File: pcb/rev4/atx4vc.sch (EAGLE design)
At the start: 58 parts, among them IC1 MY_7905DT, IC2 MAX486X/SOT, J2 ATX24RH

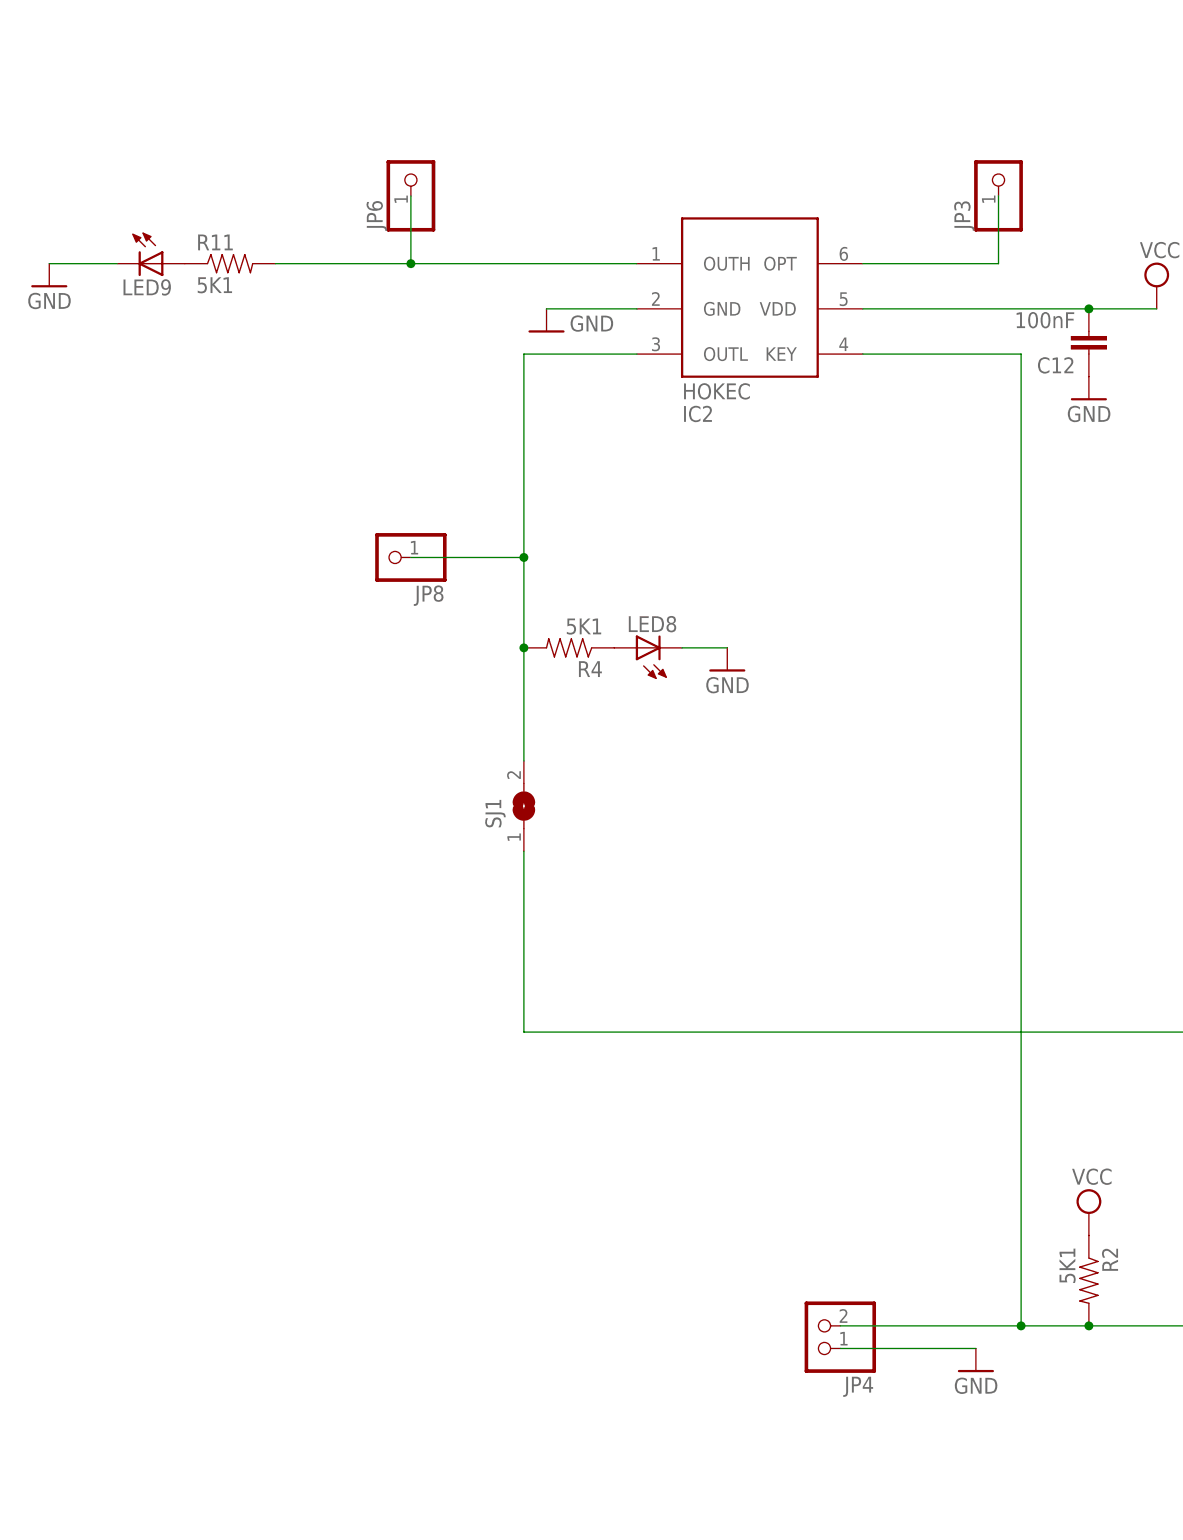
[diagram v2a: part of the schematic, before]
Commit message: soft power ic tested working
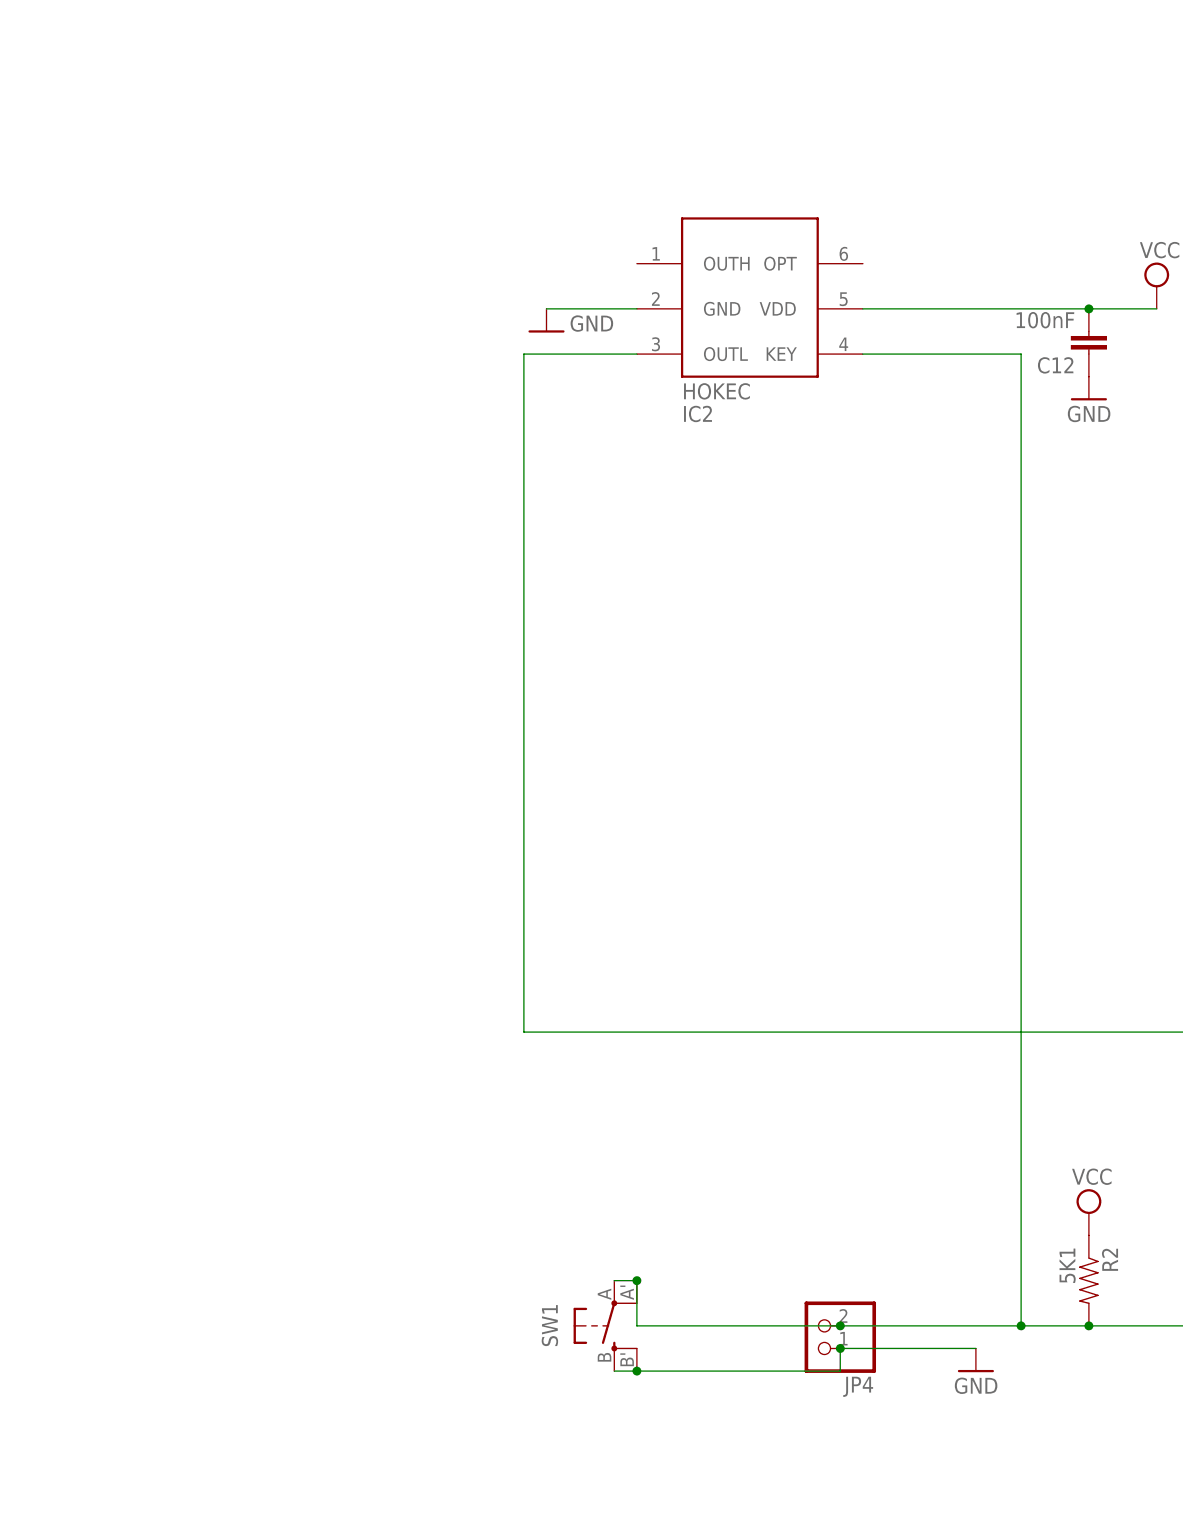
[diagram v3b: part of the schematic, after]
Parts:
- removed JP3, JP6, JP8: (no value), adafruit_changed:PINHD-1X1CB
- removed LED8, LED9: (no value), adafruit:LEDCHIP-LED0805
- removed R11, R4: 5K1, atx_power_control:RESISTOR0805-RES
- removed SJ1: (no value), jumper:SJ
- added SW1: SPST_TACT-EVQQ2, duckypad:SPST_TACT-EVQQ2
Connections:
- removed net N$13: LED8.A, R4.1
- removed net N$16: LED9.A, R11.1
- removed net N$19: IC2.OUTL, JP8.1, R4.2, SJ1.2
- removed net N$3: IC2.OPT, JP3.1
- removed net N$7: IC2.OUTH, JP6.1, R11.2
- net GND: now also SW1.S, SW1.S1; no longer LED8.C, LED9.C
- net N$12: now also SW1.P, SW1.P1
- net N$6: now also IC2.OUTL; no longer SJ1.1
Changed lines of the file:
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@@
 <part name="R2" library="atx_power_control" deviceset="RESISTOR" device="0805-RES" value="5K1"/>
 <part name="SUPPLY7" library="supply2" library_urn="urn:adsk.eagle:library:372" deviceset="VCC" device=""/>
-<part name="R4" library="atx_power_control" deviceset="RESISTOR" device="0805-RES" value="5K1"/>
-<part name="LED8" library="adafruit" deviceset="LED" device="CHIP-LED0805"/>
-<part name="GND27" library="supply1" deviceset="GND" device=""/>
-<part name="R11" library="atx_power_control" deviceset="RESISTOR" device="0805-RES" value="5K1"/>
-<part name="LED9" library="adafruit" deviceset="LED" device="CHIP-LED0805"/>
-<part name="GND28" library="supply1" deviceset="GND" device=""/>
-<part name="JP6" library="adafruit_changed" deviceset="PINHD-1X1" device="CB"/>
-<part name="JP8" library="adafruit_changed" deviceset="PINHD-1X1" device="CB"/>
-<part name="SJ1" library="jumper" library_urn="urn:adsk.eagle:library:252" deviceset="SJ" device="" package3d_urn="urn:adsk.eagle:package:15471/1"/>
-<part name="JP3" library="adafruit_changed" deviceset="PINHD-1X1" device="CB"/>
+<part name="SW1" library="duckypad" deviceset="SPST_TACT" device="-EVQQ2"/>
 </parts>
 <sheets>
@@
 <attribute name="VALUE" x="158.115" y="-19.685" size="1.778" layer="96"/>
 </instance>
-<instance part="R4" gate="G$1" x="101.6" y="40.64" smashed="yes" rot="R180">
-<attribute name="NAME" x="105.41" y="39.1414" size="1.778" layer="95" rot="R180"/>
-<attribute name="VALUE" x="105.41" y="43.942" size="1.778" layer="96" rot="R180"/>
-</instance>
-<instance part="LED8" gate="G$1" x="109.22" y="40.64" smashed="yes" rot="R90">
-<attribute name="NAME" x="113.792" y="44.196" size="1.778" layer="95" rot="R180"/>
-<attribute name="VALUE" x="113.792" y="46.355" size="1.778" layer="96" rot="R180"/>
-</instance>
-<instance part="GND27" gate="1" x="119.38" y="38.1" smashed="yes" rot="MR0">
-<attribute name="VALUE" x="121.92" y="35.56" size="1.778" layer="96" rot="MR0"/>
-</instance>
-<instance part="R11" gate="G$1" x="63.5" y="83.82" smashed="yes">
-<attribute name="NAME" x="59.69" y="85.3186" size="1.778" layer="95"/>
-<attribute name="VALUE" x="59.69" y="80.518" size="1.778" layer="96"/>
-</instance>
-<instance part="LED9" gate="G$1" x="55.88" y="83.82" smashed="yes" rot="R270">
-<attribute name="NAME" x="51.308" y="80.264" size="1.778" layer="95"/>
-<attribute name="VALUE" x="51.308" y="78.105" size="1.778" layer="96"/>
-</instance>
-<instance part="GND28" gate="1" x="43.18" y="81.28" smashed="yes" rot="MR0">
-<attribute name="VALUE" x="45.72" y="78.74" size="1.778" layer="96" rot="MR0"/>
-</instance>
-<instance part="JP6" gate="G$1" x="83.82" y="93.98" smashed="yes" rot="R90">
-<attribute name="NAME" x="80.645" y="87.63" size="1.778" layer="95" rot="R90"/>
-<attribute name="VALUE" x="88.9" y="87.63" size="1.778" layer="96" rot="R90"/>
-</instance>
-<instance part="JP8" gate="G$1" x="81.28" y="50.8" smashed="yes" rot="R180">
-<attribute name="NAME" x="87.63" y="47.625" size="1.778" layer="95" rot="R180"/>
-<attribute name="VALUE" x="87.63" y="55.88" size="1.778" layer="96" rot="R180"/>
-</instance>
-<instance part="SJ1" gate="1" x="96.52" y="22.86" smashed="yes" rot="R90">
-<attribute name="NAME" x="93.98" y="20.32" size="1.778" layer="95" rot="R90"/>
-<attribute name="VALUE" x="100.33" y="20.32" size="1.778" layer="96" rot="R90"/>
-</instance>
-<instance part="JP3" gate="G$1" x="149.86" y="93.98" smashed="yes" rot="R90">
-<attribute name="NAME" x="146.685" y="87.63" size="1.778" layer="95" rot="R90"/>
-<attribute name="VALUE" x="154.94" y="87.63" size="1.778" layer="96" rot="R90"/>
+<instance part="SW1" gate="G$1" x="106.68" y="-35.56" smashed="yes" rot="MR180">
+<attribute name="NAME" x="100.33" y="-33.02" size="1.778" layer="95" rot="MR270"/>
 </instance>
 </instances>
@@
 <pinref part="JP4" gate="G$1" pin="1"/>
 <wire x1="147.32" y1="-38.1" x2="132.08" y2="-38.1" width="0.1524" layer="91"/>
+<pinref part="SW1" gate="G$1" pin="S"/>
+<pinref part="SW1" gate="G$1" pin="S1"/>
+<wire x1="106.68" y1="-40.64" x2="109.22" y2="-40.64" width="0.1524" layer="91"/>
+<wire x1="132.08" y1="-38.1" x2="132.08" y2="-40.64" width="0.1524" layer="91"/>
+<wire x1="132.08" y1="-40.64" x2="109.22" y2="-40.64" width="0.1524" layer="91"/>
+<junction x="132.08" y="-38.1"/>
+<junction x="109.22" y="-40.64"/>
 </segment>
 <segment>
@@
 <pinref part="C12" gate="G$1" pin="1"/>
 <pinref part="GND25" gate="1" pin="GND"/>
-</segment>
-<segment>
-<pinref part="LED8" gate="G$1" pin="C"/>
-<pinref part="GND27" gate="1" pin="GND"/>
-<wire x1="119.38" y1="40.64" x2="114.3" y2="40.64" width="0.1524" layer="91"/>
-</segment>
-<segment>
-<pinref part="LED9" gate="G$1" pin="C"/>
-<pinref part="GND28" gate="1" pin="GND"/>
-<wire x1="43.18" y1="83.82" x2="50.8" y2="83.82" width="0.1524" layer="91"/>
 </segment>
 </net>
@@
 </segment>
 </net>
-<net name="N$3" class="0">
-<segment>
-<pinref part="IC2" gate="G$1" pin="OPT"/>
-<wire x1="149.86" y1="91.44" x2="149.86" y2="83.82" width="0.1524" layer="91"/>
-<wire x1="149.86" y1="83.82" x2="134.62" y2="83.82" width="0.1524" layer="91"/>
-<pinref part="JP3" gate="G$1" pin="1"/>
-</segment>
-</net>
 <net name="N$6" class="0">
 <segment>
@@
 <pinref part="JP7" gate="A" pin="1"/>
 <wire x1="172.72" y1="-30.48" x2="182.88" y2="-30.48" width="0.1524" layer="91"/>
-<wire x1="96.52" y1="17.78" x2="96.52" y2="-2.54" width="0.1524" layer="91"/>
-<pinref part="SJ1" gate="1" pin="1"/>
-</segment>
-</net>
-<net name="N$7" class="0">
-<segment>
-<pinref part="IC2" gate="G$1" pin="OUTH"/>
-<wire x1="109.22" y1="83.82" x2="83.82" y2="83.82" width="0.1524" layer="91"/>
-<pinref part="R11" gate="G$1" pin="2"/>
-<pinref part="JP6" gate="G$1" pin="1"/>
-<wire x1="83.82" y1="83.82" x2="68.58" y2="83.82" width="0.1524" layer="91"/>
-<wire x1="83.82" y1="91.44" x2="83.82" y2="83.82" width="0.1524" layer="91"/>
-<junction x="83.82" y="83.82"/>
+<pinref part="IC2" gate="G$1" pin="OUTL"/>
+<wire x1="109.22" y1="73.66" x2="96.52" y2="73.66" width="0.1524" layer="91"/>
+<wire x1="96.52" y1="73.66" x2="96.52" y2="-2.54" width="0.1524" layer="91"/>
 </segment>
 </net>
@@
 <wire x1="152.4" y1="73.66" x2="134.62" y2="73.66" width="0.1524" layer="91"/>
 <junction x="152.4" y="-35.56"/>
-</segment>
-</net>
-<net name="N$13" class="0">
-<segment>
-<pinref part="R4" gate="G$1" pin="1"/>
-<pinref part="LED8" gate="G$1" pin="A"/>
-</segment>
-</net>
-<net name="N$16" class="0">
-<segment>
-<pinref part="R11" gate="G$1" pin="1"/>
-<pinref part="LED9" gate="G$1" pin="A"/>
-</segment>
-</net>
-<net name="N$19" class="0">
-<segment>
-<pinref part="IC2" gate="G$1" pin="OUTL"/>
-<wire x1="109.22" y1="73.66" x2="96.52" y2="73.66" width="0.1524" layer="91"/>
-<wire x1="96.52" y1="73.66" x2="96.52" y2="50.8" width="0.1524" layer="91"/>
-<pinref part="JP8" gate="G$1" pin="1"/>
-<wire x1="83.82" y1="50.8" x2="96.52" y2="50.8" width="0.1524" layer="91"/>
-<junction x="96.52" y="50.8"/>
-<wire x1="96.52" y1="50.8" x2="96.52" y2="40.64" width="0.1524" layer="91"/>
-<pinref part="R4" gate="G$1" pin="2"/>
-<junction x="96.52" y="40.64"/>
-<wire x1="96.52" y1="40.64" x2="96.52" y2="27.94" width="0.1524" layer="91"/>
-<pinref part="SJ1" gate="1" pin="2"/>
-</segment>
-</net>
+<pinref part="SW1" gate="G$1" pin="P"/>
+<pinref part="SW1" gate="G$1" pin="P1"/>
+<wire x1="106.68" y1="-30.48" x2="109.22" y2="-30.48" width="0.1524" layer="91"/>
+<wire x1="132.08" y1="-35.56" x2="109.22" y2="-35.56" width="0.1524" layer="91"/>
+<wire x1="109.22" y1="-35.56" x2="109.22" y2="-30.48" width="0.1524" layer="91"/>
+<junction x="132.08" y="-35.56"/>
+<junction x="109.22" y="-30.48"/>
+</segment>
+</net>

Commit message: finishing touches
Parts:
- R3: value 470 -> 330
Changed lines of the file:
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@@
 <part name="GND24" library="supply1" deviceset="GND" device=""/>
 <part name="GND32" library="supply1" deviceset="GND" device=""/>
-<part name="R3" library="atx_power_control" deviceset="RESISTOR" device="0805-RES" value="470"/>
+<part name="R3" library="atx_power_control" deviceset="RESISTOR" device="0805-RES" value="330"/>
 <part name="JP2" library="pinhead" library_urn="urn:adsk.eagle:library:325" deviceset="PINHD-1X2" device="" package3d_urn="urn:adsk.eagle:package:22435/2"/>
 <part name="GND31" library="supply1" deviceset="GND" device=""/>
